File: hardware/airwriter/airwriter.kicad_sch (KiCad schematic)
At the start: 48 parts, among them J1 USB-C 5V in, J2 Mini-DIN-8 to printer, J3 Bring-up USB/UART, J4 Mini-DIN-8 LocalTalk, J5 ICSP, SW1 CONFIG/BOOT, U1 ESP32-S3-WROOM-1-N8R2, U2 MAX3490ESA+, U3 MAX3232ESE+, U4 AP7361C-33E, U5 USBLC6-2SC6, U6 SP3485EN-L, U7 PIC12F1840-I/SN, U8 SP3485EN-L

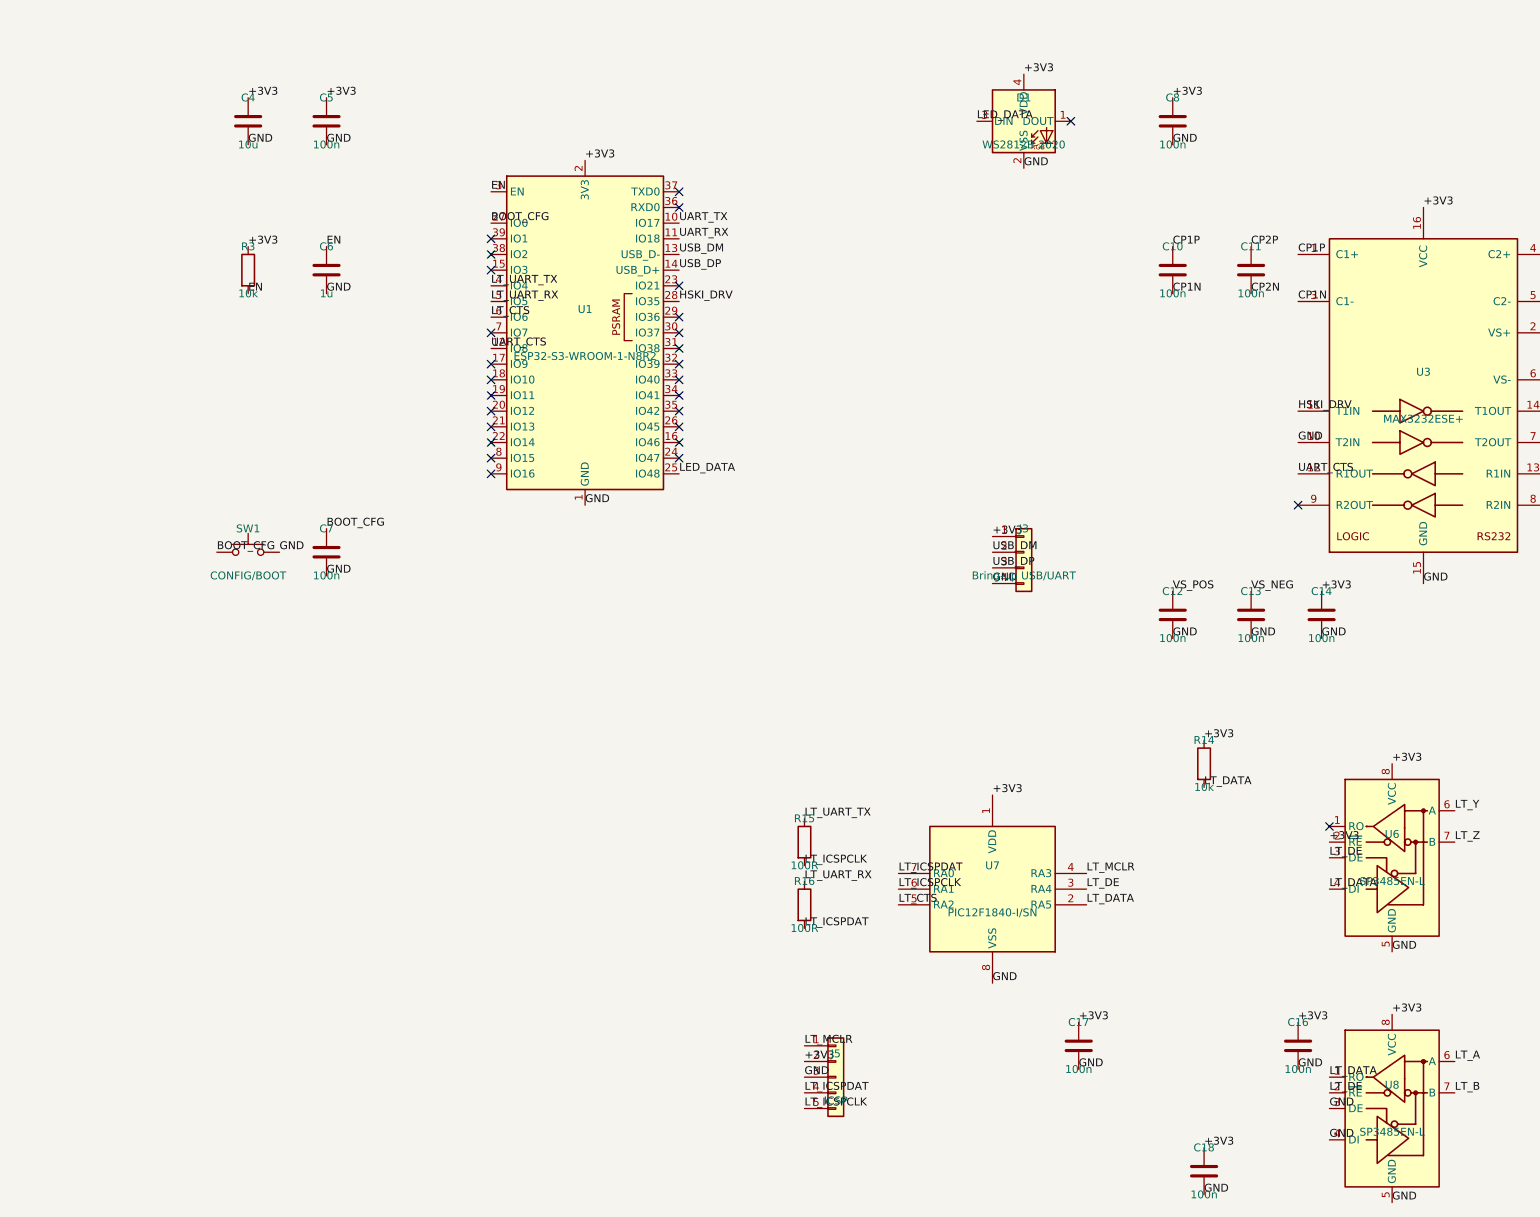
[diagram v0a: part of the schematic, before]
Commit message: Add status LEDs, mode button and I2C header to the schematic
D2 chains off D1's DOUT, so the second addressable LED costs no GPIO —
one LED can show network state while the other shows the printer link,
which a single RGB has to serialise into blink codes.

D3 is a plain green LED across the 3V3 rail with no GPIO at all. During
bring-up it separates 'board is dead' from 'firmware is dead'.

SW2 sits on IO14 rather than sharing IO0 with SW1: IO0 is a strapping
pin, so holding it at reset means USB download mode and it cannot also
mean 'hold to do something else'. C19 mirrors the SW1/C7 debounce.

J6 is a 4-pin JST-SH on IO15/IO16 with 4.7k pullups, Qwiic pin order.
A display module plugs in if one is ever wanted; the board does not
commit 27x27mm to a screen that may never be fitted.

ERC clean. The four lib_symbol_mismatch warnings are pre-existing on
U6/U8/J2/J4 and untouched here.
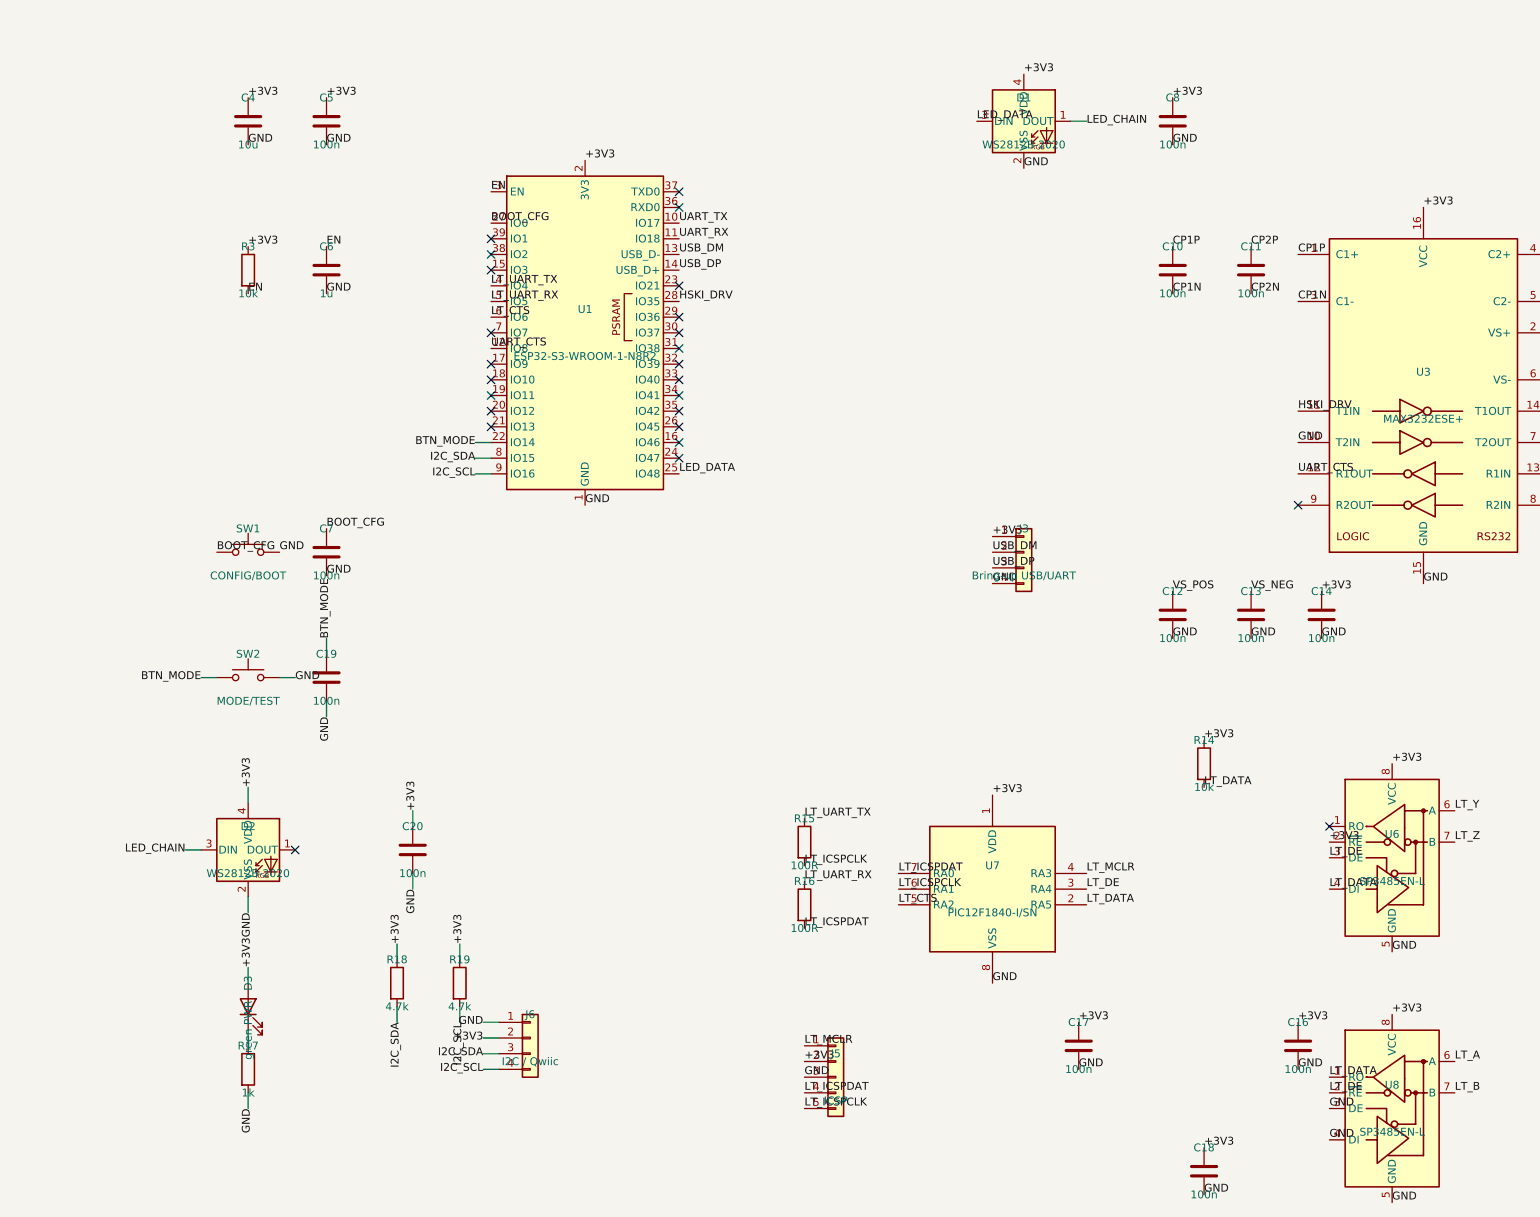
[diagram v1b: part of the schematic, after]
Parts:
- added C19, C20: 100n, Capacitor_SMD:C_0603_1608Metric, symbol Device:C
- added D2: WS2812B-2020, LED_SMD:LED_WS2812B-2020_PLCC4_2.0x2.0mm, symbol LED:WS2812B-2020
- added D3: green PWR, LED_SMD:LED_0603_1608Metric, symbol Device:LED
- added J6: I2C / Qwiic, Connector_JST:JST_SH_SM04B-SRSS-TB_1x04-1MP_P1.00mm_Horizontal, symbol Connector_Generic:Conn_01x04
- added R17: 1k, Resistor_SMD:R_0603_1608Metric, symbol Device:R
- added R18, R19: 4.7k, Resistor_SMD:R_0603_1608Metric, symbol Device:R
- added SW2: MODE/TEST, Button_Switch_SMD:SW_SPST_B3U-1000P, symbol Switch:SW_Push
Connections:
- net +3V3: now also C20.1, D2.4 (VDD), D3.2 (A), J6.2 (Pin_2), R18.1, R19.1
- net GND: now also C19.2, C20.2, D2.2 (VSS), J6.1 (Pin_1), R17.2, SW2.2
- net BTN_MODE: now reaches U1.22 (IO14)
- net BTN_MODE: now also C19.1, SW2.1
- net I2C_SDA: now reaches U1.8 (IO15)
- net I2C_SDA: now also J6.3 (Pin_3), R18.2
- net I2C_SCL: now reaches U1.9 (IO16)
- net I2C_SCL: now also J6.4 (Pin_4), R19.2
- net LED_CHAIN: now reaches D1.1 (DOUT)
- net LED_CHAIN: now also D2.3 (DIN)
- new net: D3.1 (K), R17.1
- no-connect marks 43 -> 40

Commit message: Move the new IO to pads on U1's near edge
IO14/15/16 were picked before checking where they physically land: IO15
and IO16 come out on the WROOM's far-left edge, which would have meant
40mm runs across the densest part of the board to reach a connector in
the top-right corner.

IO36/37/38 sit on U1's right edge facing the new block, roughly 23mm
away with an open corridor. Available because the module is an N8R2 with
quad PSRAM, where GPIO33-37 are free; IO35 is already used for HSKI_DRV
on the same basis.

SDA=IO36, SCL=IO37, button=IO38. ERC still clean.
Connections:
- net BTN_MODE: now also U1.31 (IO38); no longer U1.22 (IO14)
- net I2C_SCL: now also U1.30 (IO37); no longer U1.9 (IO16)
- net I2C_SDA: now also U1.29 (IO36); no longer U1.8 (IO15)
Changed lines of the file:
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@@
-)
-  (no_connect
-    (at 219.71 137.16)
-)
-  (no_connect
-    (at 219.71 139.7)
-)
-  (no_connect
-    (at 219.71 142.24)
 )
   (no_connect
@@
   (no_connect
     (at 157.48 223.52)
+)
+  (no_connect
+    (at 189.23 157.48)
+)
+  (no_connect
+    (at 189.23 160.02)
+)
+  (no_connect
+    (at 189.23 162.56)
 )
   (wire
@@
   (wire
     (pts
-      (xy 189.23 157.48)
-      (xy 186.69 157.48))
-)
-  (wire
-    (pts
-      (xy 189.23 160.02)
-      (xy 186.69 160.02))
-)
-  (wire
-    (pts
-      (xy 189.23 162.56)
-      (xy 186.69 162.56))
-)
-  (wire
-    (pts
       (xy 149.86 245.11)
       (xy 149.86 242.57))
@@
       (xy 184.15 251.46))
 )
+  (wire
+    (pts
+      (xy 219.71 137.16)
+      (xy 222.25 137.16))
+)
+  (wire
+    (pts
+      (xy 219.71 139.7)
+      (xy 222.25 139.7))
+)
+  (wire
+    (pts
+      (xy 219.71 142.24)
+      (xy 222.25 142.24))
+)
   (label "VBUS"
     (at 50.8 44.45 0)
@@
     (at 162.56 201.93 270)
 )
-  (label "BTN_MODE"
-    (at 186.69 157.48 180)
-)
-  (label "I2C_SDA"
-    (at 186.69 160.02 180)
-)
-  (label "I2C_SCL"
-    (at 186.69 162.56 180)
-)
   (label "+3V3"
     (at 149.86 242.57 90)
@@
     (at 184.15 251.46 270)
 )
+  (label "I2C_SDA"
+    (at 222.25 137.16 0)
+)
+  (label "I2C_SCL"
+    (at 222.25 139.7 0)
+)
+  (label "BTN_MODE"
+    (at 222.25 142.24 0)
+)
   (symbol

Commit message: Space out the controls and cut the silkscreen back to designators
Ports move 2mm past the board edge so their faces land flush with the
outside of a printed case wall rather than flush with the PCB.

The buttons now straddle the board centreline at 122 and 130, the LEDs
open up from 3.4mm to 5mm pitch, and the two I2C pullups move out of the
space a plug needs.

Silkscreen goes back to reference designators. The functional names were
too wordy and several of them landed on top of parts. Only the controls
a user actually touches keep a word: PWR, NET and JOB over the LEDs,
BOOT and MODE over the buttons, plus the port names. Designators sit
below those parts so the two never collide.

J1 also shifted left; moving it down had put its shield pad on the corner
radius.

Fab package regenerated. DRC clean, parity clean, fully routed.
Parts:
- D2: MPN (none) -> WS2812B-2020; Manufacturer (none) -> Worldsemi
- J4: MPN (none) -> KMDGX-8S-BS; Manufacturer (none) -> Kycon
- J6: MPN (none) -> SM04B-SRSS-TB; Manufacturer (none) -> JST
- U6: MPN (none) -> SP3485EN-L/TR; Manufacturer (none) -> MaxLinear
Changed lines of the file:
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@@
+        (font
+          (size 1.27 1.27))))
+    (property "MPN" "KMDGX-8S-BS"
+      (at 439.42 229.87 0)
+      (hide yes)
+      (effects
+        (font
+          (size 1.27 1.27))))
+    (property "Manufacturer" "Kycon"
+      (at 439.42 229.87 0)
+      (hide yes)
+      (effects
+        (font
+          (size 1.27 1.27))))
+    (property "Description" "Mini-DIN 8-pin female, right angle, fully shielded"
+      (at 439.42 229.87 0)
+      (hide yes)
+      (effects
         (font
           (size 1.27 1.27))))
@@
         (font
           (size 1.27 1.27))))
+    (property "MPN" "SP3485EN-L/TR"
+      (at 335.28 224.79 0)
+      (hide yes)
+      (effects
+        (font
+          (size 1.27 1.27))))
+    (property "Manufacturer" "MaxLinear"
+      (at 335.28 224.79 0)
+      (hide yes)
+      (effects
+        (font
+          (size 1.27 1.27))))
+    (property "Description" "RS-485 half-duplex transceiver, 3.3V, SOIC-8"
+      (at 335.28 224.79 0)
+      (hide yes)
+      (effects
+        (font
+          (size 1.27 1.27))))
     (property "Datasheet" ""
       (at 335.28 224.79 0)
@@
         (font
           (size 1.27 1.27))))
+    (property "Description" "RS-485 half-duplex transceiver, 3.3V, SOIC-8"
+      (at 335.28 265.43 0)
+      (hide yes)
+      (effects
+        (font
+          (size 1.27 1.27))))
     (property "Datasheet" ""
       (at 335.28 265.43 0)
@@
         (font
           (size 1.27 1.27))))
+    (property "MPN" "WS2812B-2020"
+      (at 149.86 223.52 0)
+      (hide yes)
+      (effects
+        (font
+          (size 1.27 1.27))))
+    (property "Manufacturer" "Worldsemi"
+      (at 149.86 223.52 0)
+      (hide yes)
+      (effects
+        (font
+          (size 1.27 1.27))))
+    (property "Description" "Addressable RGB LED, 2020, chained from D1's DOUT"
+      (at 149.86 223.52 0)
+      (hide yes)
+      (effects
+        (font
+          (size 1.27 1.27))))
     (property "Datasheet" ""
       (at 149.86 223.52 0)
@@
       (at 195.58 254 0)
       (hide yes)
+      (effects
+        (font
+          (size 1.27 1.27))))
+    (property "MPN" "SM04B-SRSS-TB"
+      (at 195.58 254 0)
+      (hide yes)
+      (effects
+        (font
+          (size 1.27 1.27))))
+    (property "Manufacturer" "JST"
+      (at 195.58 254 0)
+      (hide yes)
+      (effects
+        (font
+          (size 1.27 1.27))))
+    (property "Description" "4-pin 1.00mm JST SH horizontal SMD header, Qwiic pin order"
+      (at 195.58 254 0)
+      (hide yes)

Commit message: Fill in the missing manufacturer part numbers
J4, U6, U8, U7, D2, SW2 and J6 had no MPN, which would have stalled a
turnkey quote. J5 and D3 are marked Manufacturer=Any, following the
convention J3 already used, so they read as deliberately generic rather
than forgotten.

ERC is unchanged: 4 lib_symbol_mismatch warnings, 0 errors, the same four
symbols as before. Those warnings pre-date this commit.
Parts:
- D3, J5: Manufacturer (none) -> Any
- SW2: MPN (none) -> B3U-1000P; Manufacturer (none) -> Omron
- U7: MPN (none) -> PIC12F1840-I/SN; Manufacturer (none) -> Microchip Technology
- U8: MPN (none) -> SP3485EN-L/TR; Manufacturer (none) -> MaxLinear
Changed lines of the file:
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@@
+        (font
+          (size 1.27 1.27))))
+    (property "MPN" "PIC12F1840-I/SN"
+      (at 270.51 229.87 0)
+      (hide yes)
+      (effects
+        (font
+          (size 1.27 1.27))))
+    (property "Manufacturer" "Microchip Technology"
+      (at 270.51 229.87 0)
+      (hide yes)
+      (effects
+        (font
+          (size 1.27 1.27))))
+    (property "Description" "8-bit MCU, SOIC-8, runs TashTalk LocalTalk firmware"
+      (at 270.51 229.87 0)
+      (hide yes)
+      (effects
         (font
           (size 1.27 1.27))))
@@
         (font
           (size 1.27 1.27))))
+    (property "MPN" ""
+      (at 245.11 260.35 0)
+      (hide yes)
+      (effects
+        (font
+          (size 1.27 1.27))))
+    (property "Manufacturer" "Any"
+      (at 245.11 260.35 0)
+      (hide yes)
+      (effects
+        (font
+          (size 1.27 1.27))))
+    (property "Description" "1x5 1.27mm pin header, ICSP for the PIC"
+      (at 245.11 260.35 0)
+      (hide yes)
+      (effects
+        (font
+          (size 1.27 1.27))))
     (property "Datasheet" ""
       (at 245.11 260.35 0)
@@
         (font
           (size 1.27 1.27))))
+    (property "MPN" "SP3485EN-L/TR"
+      (at 335.28 265.43 0)
+      (hide yes)
+      (effects
+        (font
+          (size 1.27 1.27))))
+    (property "Manufacturer" "MaxLinear"
+      (at 335.28 265.43 0)
+      (hide yes)
+      (effects
+        (font
+          (size 1.27 1.27))))
     (property "Description" "RS-485 half-duplex transceiver, 3.3V, SOIC-8"
       (at 335.28 265.43 0)
@@
         (font
           (size 1.27 1.27))))
+    (property "MPN" "B3U-1000P"
+      (at 149.86 195.58 0)
+      (hide yes)
+      (effects
+        (font
+          (size 1.27 1.27))))
+    (property "Manufacturer" "Omron"
+      (at 149.86 195.58 0)
+      (hide yes)
+      (effects
+        (font
+          (size 1.27 1.27))))
+    (property "Description" "Tactile switch, SMD, 4.8 x 3.4mm"
+      (at 149.86 195.58 0)
+      (hide yes)
+      (effects
+        (font
+          (size 1.27 1.27))))
     (property "Datasheet" ""
       (at 149.86 195.58 0)
@@
       (at 149.86 248.92 0)
       (hide yes)
+      (effects
+        (font
+          (size 1.27 1.27))))
+    (property "MPN" ""
+      (at 149.86 248.92 0)
+      (hide yes)
+      (effects
+        (font
+          (size 1.27 1.27))))
+    (property "Manufacturer" "Any"
+      (at 149.86 248.92 0)
+      (hide yes)
+      (effects
+        (font
+          (size 1.27 1.27))))
+    (property "Description" "Green LED, 0603, power rail indicator"
+      (at 149.86 248.92 0)
+      (hide yes)

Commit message: Check the whole BOM against LCSC stock before ordering
Every named part sources and nothing is short. Prices and stock verified today,
LCSC unless noted, recorded in the handoff sourcing table: the module, both RS-485
transceivers, the MAX3490 and MAX3232, the LDO, the ESD array, the WS2812Bs, the
USB-C, the JST SH and both Omron switches. About $13 of parts per board, $5 of
which is the two Kycon mini-DINs from Mouser.

Two things worth knowing before ordering:

  J3 and J5 are the only awkward line. LCSC does not stock 1.27mm single-row male
  headers as 1x4 or 1x5, only strips -- buy C28952 or C3408 and cut. Neither has to
  be fitted: J3 is bring-up only and the PIC can be programmed off J5's pads.

  U2 and U3 now carry the +T tape MPNs rather than the plain +. Same silicon, and
  the plain MAX3232ESE+ is $1.70 at LCSC against $0.91 for the +T. The handoff had
  already quoted the +T price, so the BOM was asking for the dearer line.

Also confirmed the WS2812B-2020 footprint, since the name says 2.0 x 2.0mm and the
part is 2.2 x 2.0mm -- the footprint draws the real 2.2mm body, and the pin order
matches the chain as wired.

ERC still four warnings, no errors, all pre-existing library symbol mismatches.
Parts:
- U2: MPN MAX3490ESA+ -> MAX3490ESA+T
- U3: MPN MAX3232ESE+ -> MAX3232ESE+T
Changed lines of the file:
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@@
         (font
           (size 1.27 1.27))))
-    (property "MPN" "MAX3490ESA+"
+    (property "MPN" "MAX3490ESA+T"
       (at 340.36 55.88 0)
       (hide yes)
@@
         (font
           (size 1.27 1.27))))
-    (property "MPN" "MAX3232ESE+"
+    (property "MPN" "MAX3232ESE+T"
       (at 340.36 146.05 0)
       (hide yes)

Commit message: Grow the board to 52 x 78mm and open a band for artwork
Twelve millimetres inserted between the ESP32 row and the transceiver row, giving a
clear 50 x 12mm strip at y 86 to 98 for a logo and whatever else wants silkscreen.
Every footprint below y=87 moved down 12mm; nothing above it moved, so the antenna
keepout, the three front connectors and their 2mm proud stand are untouched.

C9 and C14 travelled with the band rather than staying in the top row. They bypass
U2 and U3, and leaving them behind would have put them 22mm from the chips they
serve. They sit at the top edge of the lower block now, about 5mm from their pins,
which is closer than before the board grew.

The eleven footprints moved by hand for aesthetics and shorter routes are all kept
as placed -- the shift was rebuilt from the current board, not replayed from the
old placement table.

Function labels on the three internal connectors: J3 is USB, J5 is ICSP, J6 is I2C.
Per-pin labels do not fit. J3 has 1.35mm between the board edge and U1's pads, and
J6's 1mm pitch cannot hold text at the 0.8mm minimum height with legal spacing. J6
is wired in Qwiic order -- GND, 3V3, SDA, SCL -- so the word is the pinout.

Mounting holes stay non-plated, no ground ring. Nothing to bond to in a printed
case, and it would add a second path to ground that R8 could not lift.

Re-routed from scratch and re-stitched: 53 stitching vias, 18 front pour fragments
down to 7 unjoined. DRC is 3 violations, all known -- the USB-C footprint puts silk
under the board edge, and U1 mismatches its library because of the 0.30mm vias.
Drill floor still 0.300mm. Fab package regenerated.
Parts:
- U2: MPN MAX3490ESA+T -> MAX3490ESA+
- U3: MPN MAX3232ESE+T -> MAX3232ESE+
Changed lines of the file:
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@@
         (font
           (size 1.27 1.27))))
-    (property "MPN" "MAX3490ESA+T"
+    (property "MPN" "MAX3490ESA+"
       (at 340.36 55.88 0)
       (hide yes)
@@
         (font
           (size 1.27 1.27))))
-    (property "MPN" "MAX3232ESE+T"
+    (property "MPN" "MAX3232ESE+"
       (at 340.36 146.05 0)
       (hide yes)
